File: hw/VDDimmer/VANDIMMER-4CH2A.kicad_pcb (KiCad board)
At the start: 4 copper layers, 100 x 84 mm, 98 parts, among them J1 USB-C 16P, J10 A2 V+SEL VIN/5V, J11 BTN1, J12 BTN2, J13 EXP 3V3/GND/SDA/SCL/EN/IO0, J14 UART1 3V3/GND/TX/RX, J2 VIN 12V, J3 CH1 LED-/V+, J4 CH2 LED-/V+, J5 CH3 LED-/V+, J6 CH4 LED-/V+, J7 ADDR1 V+/D/CLK/GND, J8 ADDR2 V+/D/CLK/GND, J9 A1 V+SEL VIN/5V, Q1 20N06, Q2 20N06, Q3 20N06, Q4 20N06, Q5 SUD50P06-15, U1 ESP32-S3-WROOM-1-N16R8, U2 AP63301WU-7, U3 BL1117-33CX, U4 74HCT125, U5 74HCT125

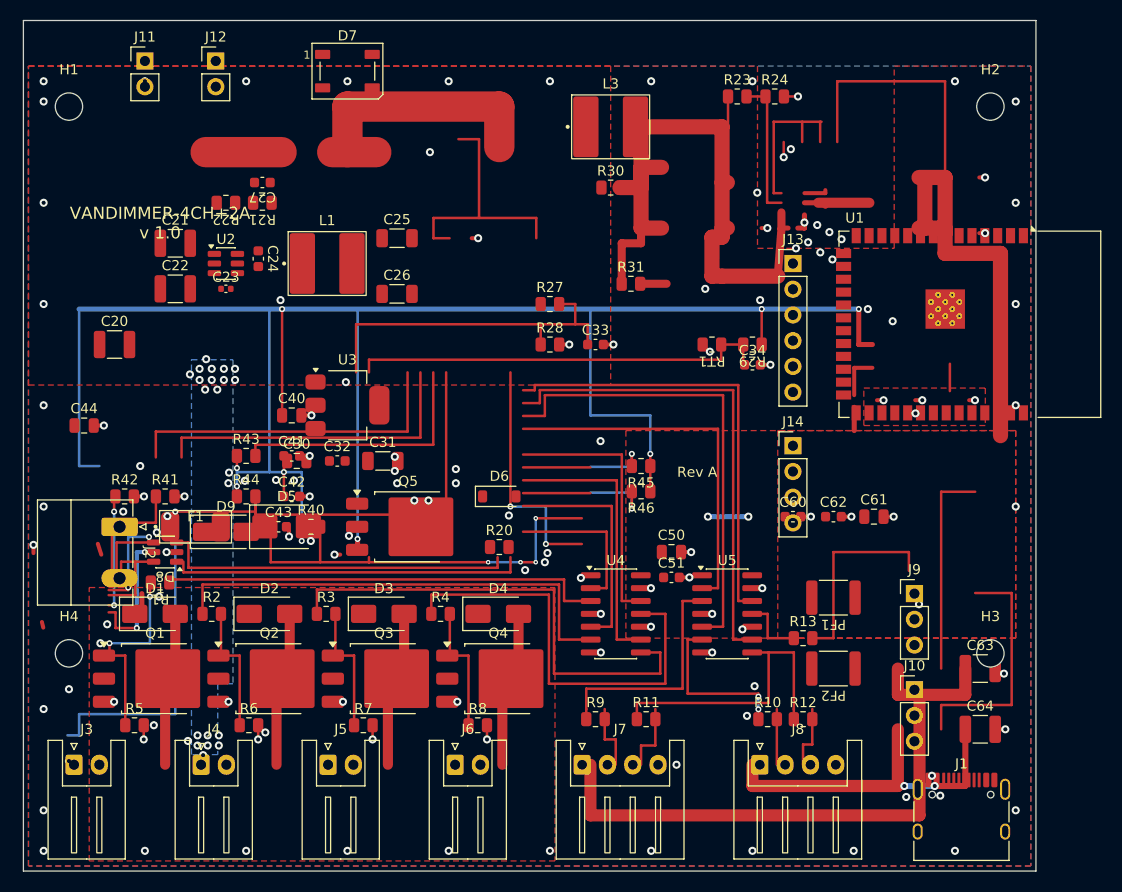
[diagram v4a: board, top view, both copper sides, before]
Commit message: Place remaining components
All 98 footprints are now placed and fpspace.py --courtyards reports ZERO
overlaps, exit 0 - the gate the plan sets for this task.

Q1-Q4 sit between U4 and the J3-J6 connectors at 11.3 mm pitch, with D1-D4
above them and the gate resistors R1-R8 below, so each drain run to its
connector and each gate run from U4 stays short. The block is right-shifted to
x 108.57..153.65 rather than aligned per-channel with J3-J6: H4's 5.90 mm
keepout occupies the bottom-left corner that channel 1 would otherwise want,
and the hole has to be there to do the J2-to-J3 separation job spec section
5.1 gives it.

RT1 sits 3.62 mm from Q4 so it actually senses FET heat, which is the point of
a thermal derate.

U1's decoupling (C40-C44) is packed into the x 168..172 column, 9-12 mm from
the module pads rather than the 3-5 mm the plan asks for. That is forced, not
sloppy: U1's courtyard blocks every position closer, and courtyards_overlap is
an error in this project. Flagging it as a routing constraint - these want
short, wide vias straight to the In1.Cu GND plane, which the 4-layer stackup
now makes cheap.

A final D1-vs-J2 overlap of 0.300 x 3.500 mm was cleared by moving D1 right to
x 116. J2 could not move left instead: at x 108.5 its courtyard crosses the
x=100 board edge.

crtyd.py only lists courtyards, it never tests them against Edge.Cuts, so the
plan's "every courtyard inside Edge.Cuts except U1" expectation was checked
separately: exactly one footprint leaves the outline, U1, whose antenna
overhangs by design per spec decision 5.

Hot loop re-measured after all placement: still 2.51 mm2, 0 vias inside.

Co-Authored-By: Claude Opus 5 (1M context) <noreply@anthropic.com>
Claude-Session: https://claude.ai/code/session_01YZHVU8aymL4RkLeCfwomwj
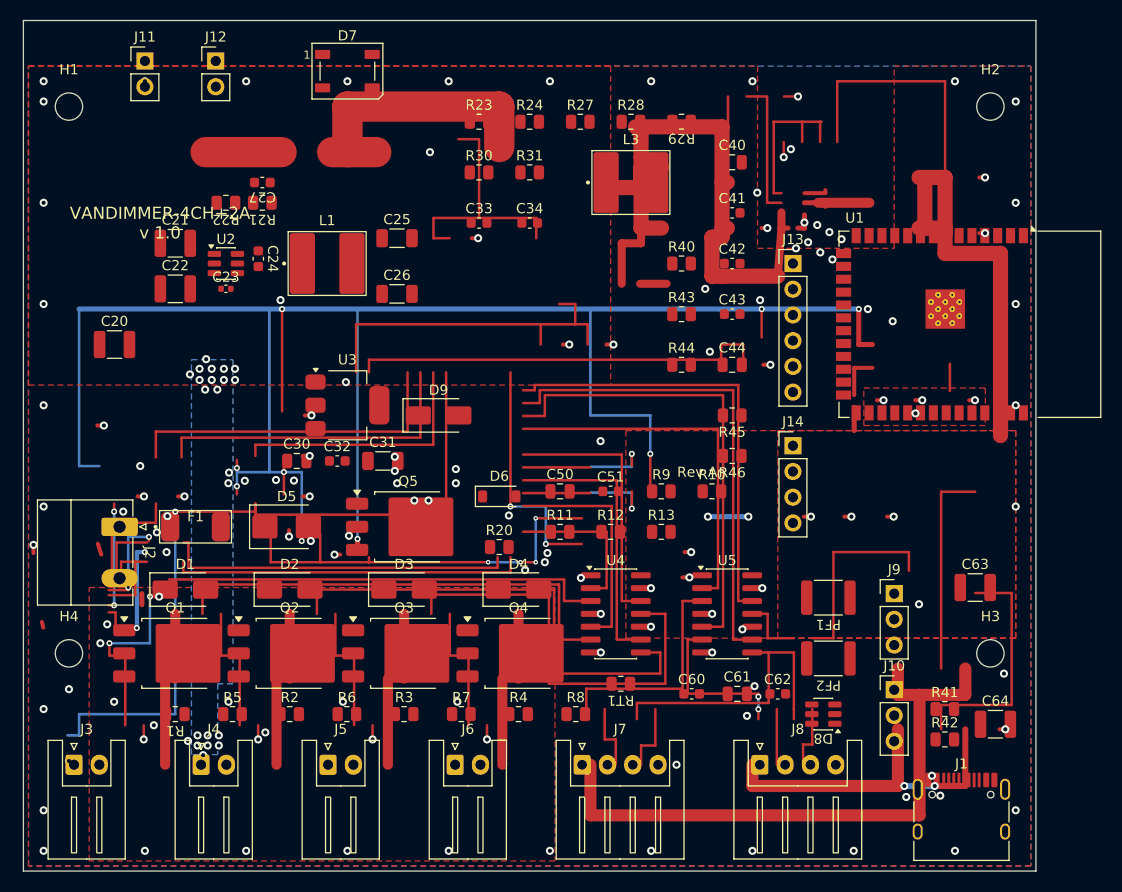
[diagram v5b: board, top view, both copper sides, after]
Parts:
- moved R42 84.5 mm to (191.0, 127.0)
- moved R41 79.8 mm to (191.0, 124.0)
- moved D8 66.9 mm to (179.0, 124.5)
- moved C44 64.3 mm to (170.0, 90.0)
- moved C40 50.2 mm to (170.0, 70.0)
- moved C41 49.7 mm to (170.0, 75.0)
- moved C43 49.5 mm to (170.0, 85.0)
- moved C42 49.2 mm to (170.0, 80.0)
- moved R43 45.2 mm to (165.0, 85.0)
- moved R44 44.9 mm to (165.0, 90.0)
- moved R40 44.9 mm to (165.0, 80.0)
- moved RT1 34.7 mm to (159.0, 121.5)
- moved R12 26.5 mm to (158.0, 106.5)
- moved C34 26.1 mm to (150.0, 76.0)
- moved R23 25.6 mm to (145.0, 66.0)
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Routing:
- net /MCU/UART1_RX: track 32.0 -> 0.00 mm
- net +5V: track 109.0 -> 141.0 mm
- net /Addressable/ADDR2_VSEL: track 24.0 -> 0.00 mm
- net GND: track 55.7 -> 79.1 mm, vias 134 -> 133
- net +3V3: track 199.7 -> 200.4 mm, vias 9 -> 10

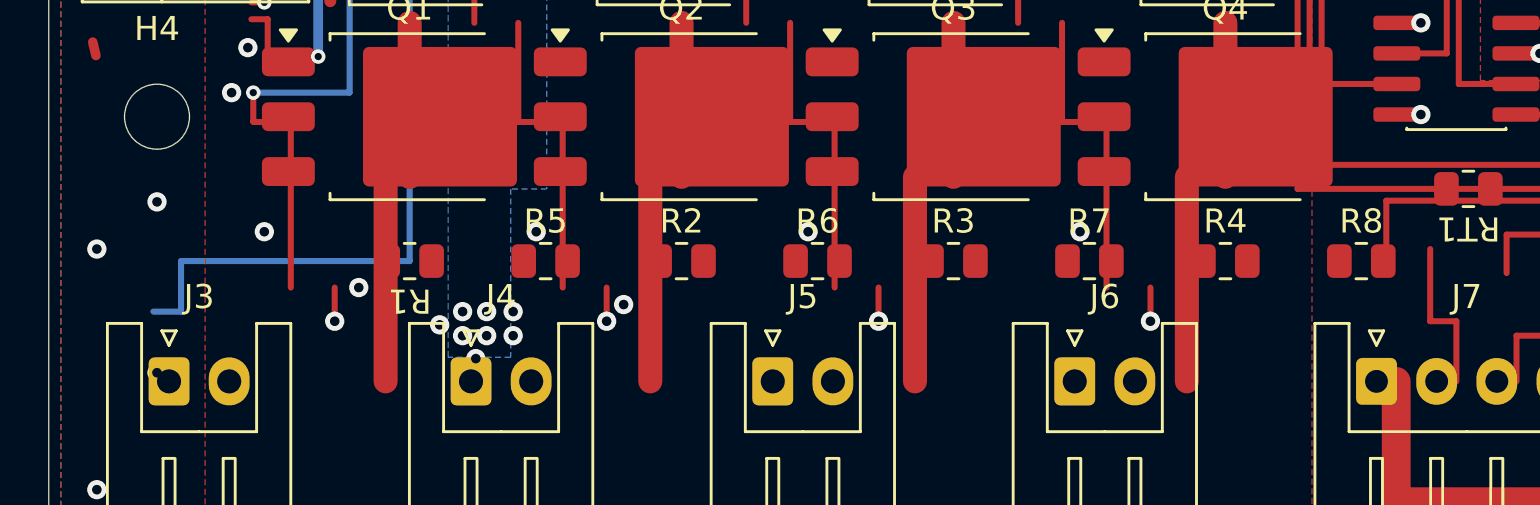
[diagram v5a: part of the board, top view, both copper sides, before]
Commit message: Widen the silk band above J3-J6 for correctly sized polarity marks
The project sets min_text_height 0.8 mm and the first pass at the J3-J6
polarity marks used 0.7 mm, which DRC flagged eight times. Correctly sized
0.8 mm text renders ~1.35 mm tall and did not fit the 1.54 mm band between the
gate-resistor row and the connector silk outline.

R1-R8 move up 0.7 mm to y 123.8, opening the band from 1.54 mm to 2.23 mm and
giving 0.44 mm clearance on each side of the text. The resistors keep 0.76 mm
to the Q1-Q4 row above them, and fpspace.py --courtyards still reports zero
overlaps.

The eight undersized marks are still on the board; they are replaced next.

Co-Authored-By: Claude Opus 5 (1M context) <noreply@anthropic.com>
Claude-Session: https://claude.ai/code/session_01YZHVU8aymL4RkLeCfwomwj
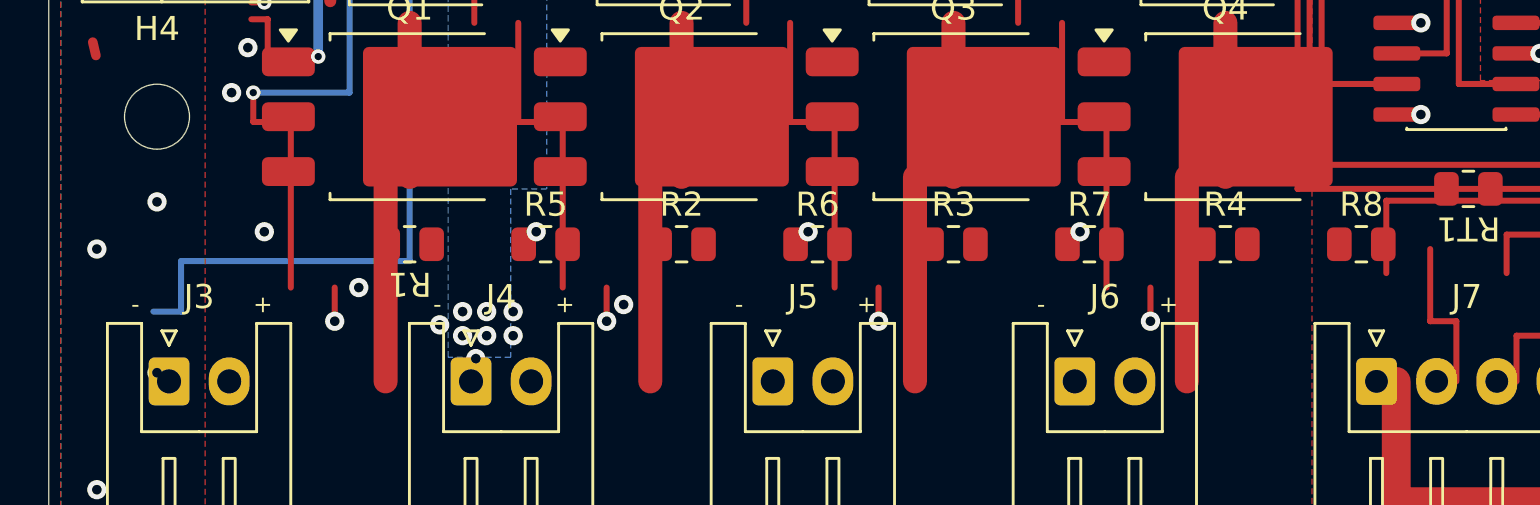
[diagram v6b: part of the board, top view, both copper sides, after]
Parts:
- moved R1 0.70 mm to (115.0, 123.8)
- moved R2 0.70 mm to (126.3, 123.8)
- moved R3 0.70 mm to (137.6, 123.8)
- moved R4 0.70 mm to (148.9, 123.8)
- moved R5 0.70 mm to (120.7, 123.8)
- moved R6 0.70 mm to (131.9, 123.8)
- moved R7 0.70 mm to (143.2, 123.8)
- moved R8 0.70 mm to (154.6, 123.8)
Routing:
- net GND: vias 133 -> 130
- net /PWM/GATE3: vias 0 -> 1
- net /PWM/GATE2: vias 0 -> 1
- net /PWM/GATE1: vias 2 -> 3
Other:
- board text added: "+"
- board text added: "-"
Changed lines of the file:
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@@
 	(footprint "Resistor_SMD:R_0805_2012Metric"
 		(layer "F.Cu")
-		(at 120.65 124.5)
+		(at 120.65 123.8)
 		(descr "Resistor SMD 0805 (2012 Metric), square (rectangular) end terminal, IPC-7351 nominal, (Body size source: IPC-SM-782 page 72, https://www.pcb-3d.com/wordpress/wp-content/uploads/ipc-sm-782a_amendment_1_and_2.pdf)")
 		(tags "resistor")
@@
 	(footprint "Resistor_SMD:R_0805_2012Metric"
 		(layer "F.Cu")
-		(at 137.6 124.5)
+		(at 137.6 123.8)
 		(descr "Resistor SMD 0805 (2012 Metric), square (rectangular) end terminal, IPC-7351 nominal, (Body size source: IPC-SM-782 page 72, https://www.pcb-3d.com/wordpress/wp-content/uploads/ipc-sm-782a_amendment_1_and_2.pdf)")
 		(tags "resistor")
@@
 	(footprint "Resistor_SMD:R_0805_2012Metric"
 		(layer "F.Cu")
-		(at 131.949999 124.5)
+		(at 131.949999 123.8)
 		(descr "Resistor SMD 0805 (2012 Metric), square (rectangular) end terminal, IPC-7351 nominal, (Body size source: IPC-SM-782 page 72, https://www.pcb-3d.com/wordpress/wp-content/uploads/ipc-sm-782a_amendment_1_and_2.pdf)")
 		(tags "resistor")
@@
 	(footprint "Resistor_SMD:R_0805_2012Metric"
 		(layer "F.Cu")
-		(at 154.55 124.5)
+		(at 154.55 123.8)
 		(descr "Resistor SMD 0805 (2012 Metric), square (rectangular) end terminal, IPC-7351 nominal, (Body size source: IPC-SM-782 page 72, https://www.pcb-3d.com/wordpress/wp-content/uploads/ipc-sm-782a_amendment_1_and_2.pdf)")
 		(tags "resistor")
@@
 	(footprint "Resistor_SMD:R_0805_2012Metric"
 		(layer "F.Cu")
-		(at 148.9 124.5)
+		(at 148.9 123.8)
 		(descr "Resistor SMD 0805 (2012 Metric), square (rectangular) end terminal, IPC-7351 nominal, (Body size source: IPC-SM-782 page 72, https://www.pcb-3d.com/wordpress/wp-content/uploads/ipc-sm-782a_amendment_1_and_2.pdf)")
 		(tags "resistor")
@@
 	(footprint "Resistor_SMD:R_0805_2012Metric"
 		(layer "F.Cu")
-		(at 126.3 124.5)
+		(at 126.3 123.8)
 		(descr "Resistor SMD 0805 (2012 Metric), square (rectangular) end terminal, IPC-7351 nominal, (Body size source: IPC-SM-782 page 72, https://www.pcb-3d.com/wordpress/wp-content/uploads/ipc-sm-782a_amendment_1_and_2.pdf)")
 		(tags "resistor")
@@
 	(footprint "Resistor_SMD:R_0805_2012Metric"
 		(layer "F.Cu")
-		(at 115 124.5 180)
+		(at 115 123.8 180)
 		(descr "Resistor SMD 0805 (2012 Metric), square (rectangular) end terminal, IPC-7351 nominal, (Body size source: IPC-SM-782 page 72, https://www.pcb-3d.com/wordpress/wp-content/uploads/ipc-sm-782a_amendment_1_and_2.pdf)")
 		(tags "resistor")
@@
 	(footprint "Resistor_SMD:R_0805_2012Metric"
 		(layer "F.Cu")
-		(at 143.25 124.5)
+		(at 143.25 123.8)
 		(descr "Resistor SMD 0805 (2012 Metric), square (rectangular) end terminal, IPC-7351 nominal, (Body size source: IPC-SM-782 page 72, https://www.pcb-3d.com/wordpress/wp-content/uploads/ipc-sm-782a_amendment_1_and_2.pdf)")
 		(tags "resistor")
@@
 		(layer "Edge.Cuts")
 	)
+	(gr_text "-"
+		(at 103.6 126.3 0)
+		(layer "F.SilkS")
+		(effects
+			(font
+				(size 0.7 0.7)
+				(thickness 0.105)
+			)
+		)
+	)
+	(gr_text "+"
+		(at 108.9 126.3 0)
+		(layer "F.SilkS")
+		(effects
+			(font
+				(size 0.7 0.7)
+				(thickness 0.105)
+			)
+		)
+	)
+	(gr_text "-"
+		(at 116.15 126.3 0)
+		(layer "F.SilkS")
+		(effects
+			(font
+				(size 0.7 0.7)
+				(thickness 0.105)
+			)
+		)
+	)
+	(gr_text "+"
+		(at 121.45 126.3 0)
+		(layer "F.SilkS")
+		(effects
+			(font
+				(size 0.7 0.7)
+				(thickness 0.105)
+			)
+		)
+	)
+	(gr_text "-"
+		(at 128.69 126.3 0)
+		(layer "F.SilkS")
+		(effects
+			(font
+				(size 0.7 0.7)
+				(thickness 0.105)
+			)
+		)
+	)
+	(gr_text "+"
+		(at 133.99 126.3 0)
+		(layer "F.SilkS")
+		(effects
+			(font
+				(size 0.7 0.7)
+				(thickness 0.105)
+			)
+		)
+	)
+	(gr_text "-"
+		(at 141.24 126.3 0)
+		(layer "F.SilkS")
+		(effects
+			(font
+				(size 0.7 0.7)
+				(thickness 0.105)
+			)
+		)
+	)
+	(gr_text "+"
+		(at 146.54 126.3 0)
+		(layer "F.SilkS")
+		(effects
+			(font
+				(size 0.7 0.7)
+				(thickness 0.105)
+			)
+		)
+	)
 	(gr_text "Rev A"
 		(at 166.55 100.6 0)
@@
 	)
 	(via
-		(at 142.86 123.28)
-		(size 0.8)
-		(drill 0.4)
-		(layers "F.Cu" "B.Cu")
-		(net "GND")
-	)
-	(via
 		(at 113.4 112.9)
 		(size 0.8)
@@
 	)
 	(via
-		(at 131.56 123.28)
-		(size 0.8)
-		(drill 0.4)
-		(layers "F.Cu" "B.Cu")
-		(net "GND")
-	)
-	(via
 		(at 198 64)
 		(size 0.8)
@@
 	)
 	(via
-		(at 120.26 123.28)
-		(size 0.8)
-		(drill 0.4)
-		(layers "F.Cu" "B.Cu")
-		(net "GND")
-	)
-	(via
 		(at 107.6 117.5)
 		(size 0.8)
@@
 		(net "/PWM/GATE1")
 	)
+	(via
+		(at 120.26 123.28)
+		(size 0.8)
+		(drill 0.4)
+		(layers "F.Cu" "B.Cu")
+		(net "/PWM/GATE1")
+	)
 	(segment
 		(start 112.5 117.5)
@@
 		(net "/PWM/GATE2")
 	)
+	(via
+		(at 131.56 123.28)
+		(size 0.8)
+		(drill 0.4)
+		(layers "F.Cu" "B.Cu")
+		(net "/PWM/GATE2")
+	)
 	(segment
 		(start 126.3 114.6)
@@
 		(net "/PWM/GATE3")
 	)
+	(via
+		(at 142.86 123.28)
+		(size 0.8)
+		(drill 0.4)
+		(layers "F.Cu" "B.Cu")
+		(net "/PWM/GATE3")
+	)
